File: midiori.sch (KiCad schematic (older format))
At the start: 48 parts, among them J1 x68000_expansion, J2 DIN-5_180degree, J3 DIN-5_180degree, J4 DIN-5_180degree, U1 74LS245, U10 74LS393, U11 74LS74, U13 H11L1, U14 7407, U15 74LS157, U2 74LS133, U3 74LS133, U4 74LS08, U5 74LS38, U6 ym3802-x, U7 74LS32, U8 74LS04, U9 74LS10, X1 CXO_DIP8, X2 CXO_DIP8

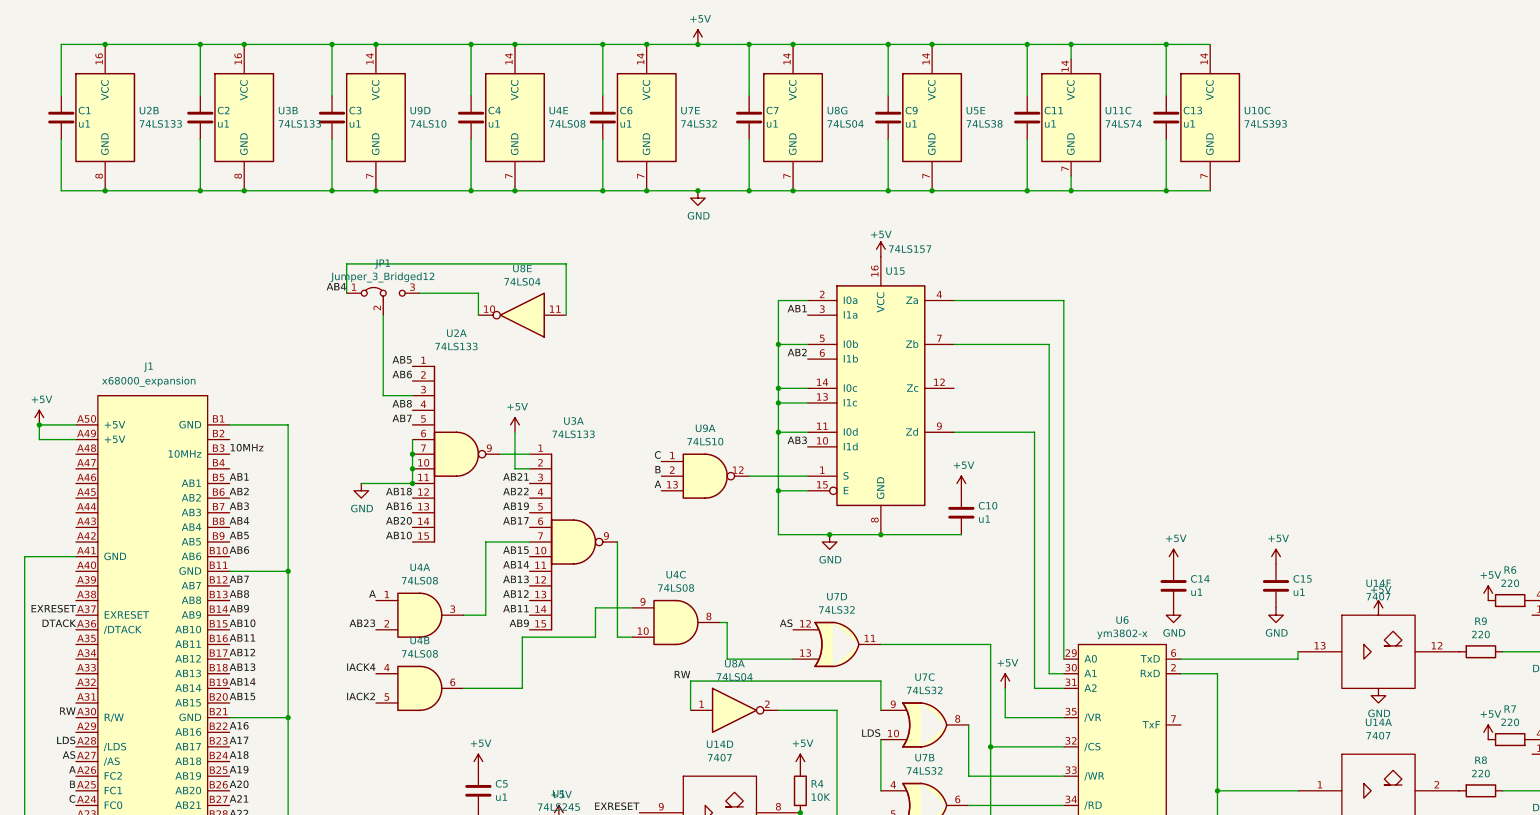
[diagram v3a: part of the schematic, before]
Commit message: Remove 74ls133 from address decoding
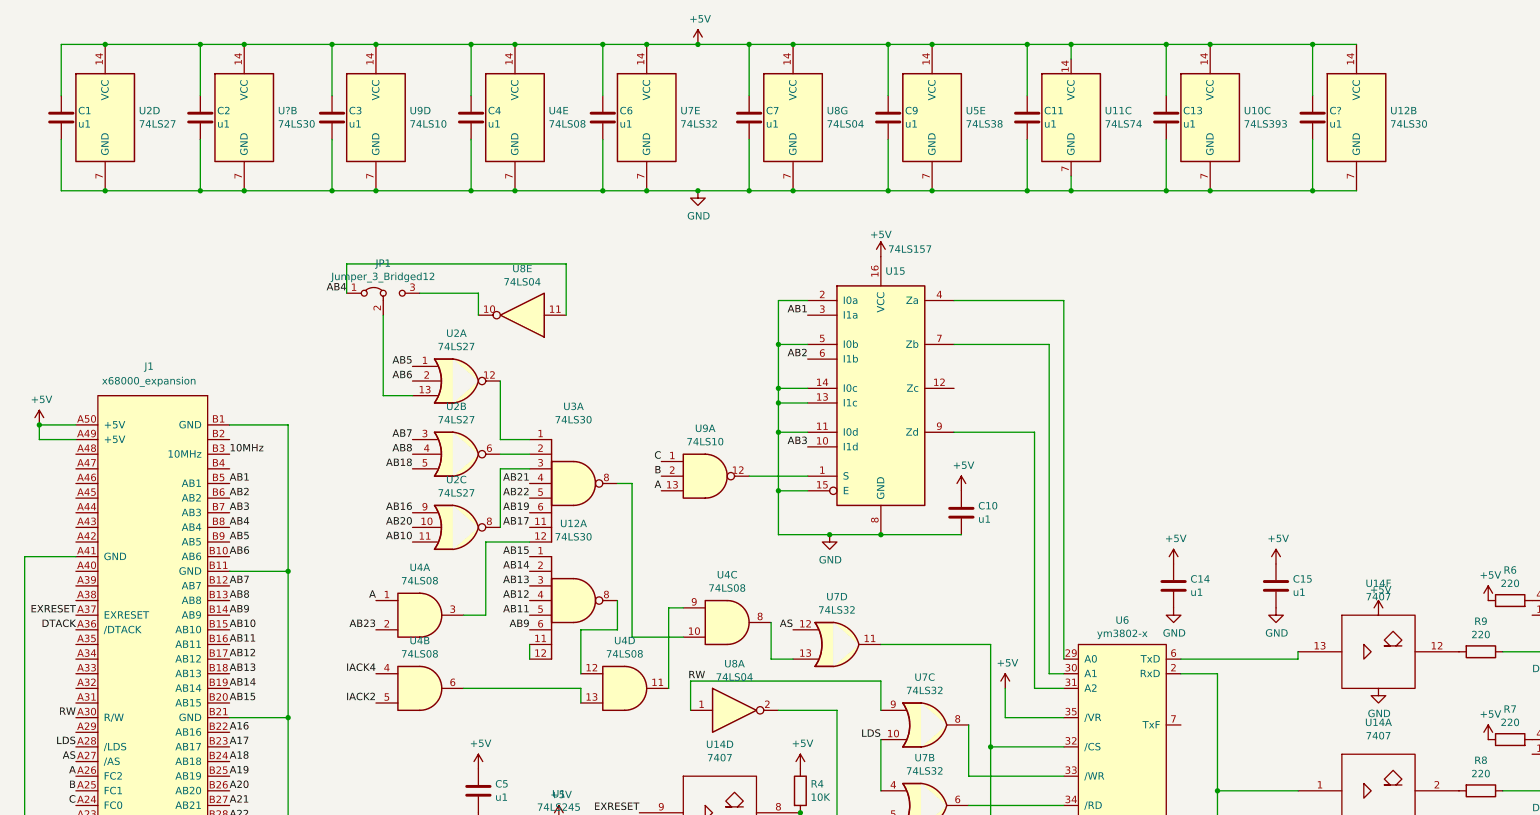
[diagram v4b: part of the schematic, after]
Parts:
- removed U2, U3: 74LS133, Package_SO:SOIC-16_3.9x9.9mm_P1.27mm, symbol 74xx:74LS133
- added C?: u1, Capacitor_SMD:C_0805_2012Metric_Pad1.15x1.40mm_HandSolder, symbol Device:C
- added U12, U3, U?: 74LS30, symbol 74xx:74LS30
- added U2: 74LS27, symbol 74xx:74LS27
- added unit 4 of U4
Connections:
- net +5V: now also C?.1, U12.14 (VCC), U2.14 (VCC), U?.14 (VCC)
- net AB10: now also U2.11
- net AB11: now also U12.5
- net AB12: now also U12.4
- net AB13: now also U12.3
- net AB14: now also U12.2
- net AB15: now also U12.1
- net AB16: now also U2.9
- net AB17: now also U3.11
- net AB18: now also U2.5
- net AB19: now also U3.6
- net AB20: now also U2.10
- net AB21: now also U3.4
- net AB22: now also U3.5
- net AB5: now also U2.1
- net AB6: now also U2.2
- net AB7: now also U2.3
- net AB8: now also U2.4
- net AB9: now also U12.6
- net GND: now also C?.2, U12.7 (GND), U2.7 (GND), U?.7 (GND)
- net at U4.3: now also U3.12
- net at U4.10: now also U3.8
- net at JP1.2 (C): now also U2.13
- net at U4.6: now also U4.13; no longer U4.9
- new net: U4.11, U4.9
- new net: U2.12, U3.1
- new net: U2.6, U3.2
- new net: U2.8, U3.3
- new net: U12.11, U12.12
- new net: U12.8, U4.12
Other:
- moved on the sheet: U4C
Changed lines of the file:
@@
 Text Label 4050 7050 2    50   ~ 0
 DB0
-$Comp
-L 74xx:74LS133 U3
-U 1 1 5BFE5824
-P 4650 4150
-F 0 "U3" H 4650 4975 50  0000 C CNN
-F 1 "74LS133" H 4650 4884 50  0000 C CNN
-F 2 "Package_SO:SOIC-16_3.9x9.9mm_P1.27mm" H 4650 4150 50  0001 C CNN
-F 3 "http://www.ti.com/lit/gpn/sn74LS133" H 4650 4150 50  0001 C CNN
-	1    4650 4150
-	1    0    0    -1
-$EndComp
-$Comp
-L 74xx:74LS133 U2
-U 2 1 5BFE5AAA
-P 1450 1250
-F 0 "U2" H 1680 1296 50  0000 L CNN
-F 1 "74LS133" H 1680 1205 50  0000 L CNN
-F 2 "Package_SO:SOIC-16_3.9x9.9mm_P1.27mm" H 1450 1250 50  0001 C CNN
-F 3 "http://www.ti.com/lit/gpn/sn74LS133" H 1450 1250 50  0001 C CNN
-	2    1450 1250
-	1    0    0    -1
-$EndComp
-$Comp
-L 74xx:74LS133 U2
-U 1 1 5BFE5C09
-P 3850 3550
-F 0 "U2" H 3850 4375 50  0000 C CNN
-F 1 "74LS133" H 3850 4284 50  0000 C CNN
-F 2 "Package_SO:SOIC-16_3.9x9.9mm_P1.27mm" H 3850 3550 50  0001 C CNN
-F 3 "http://www.ti.com/lit/gpn/sn74LS133" H 3850 3550 50  0001 C CNN
-	1    3850 3550
-	1    0    0    -1
-$EndComp
-$Comp
-L 74xx:74LS133 U3
-U 2 1 5BFE5CB5
-P 2400 1250
-F 0 "U3" H 2630 1296 50  0000 L CNN
-F 1 "74LS133" H 2630 1205 50  0000 L CNN
-F 2 "Package_SO:SOIC-16_3.9x9.9mm_P1.27mm" H 2400 1250 50  0001 C CNN
-F 3 "http://www.ti.com/lit/gpn/sn74LS133" H 2400 1250 50  0001 C CNN
-	2    2400 1250
-	1    0    0    -1
-$EndComp
 Text Label 3550 2950 2    50   ~ 0
 AB5
@@
 Text Label 3100 2450 2    50   ~ 0
 AB4
-Text Label 3550 3250 2    50   ~ 0
+Text Label 3550 3550 2    50   ~ 0
 AB8
-Text Label 3550 3350 2    50   ~ 0
+Text Label 3550 3450 2    50   ~ 0
 AB7
 Text Label 3550 4150 2    50   ~ 0
@@
 Text Label 3550 3950 2    50   ~ 0
 AB16
-Text Label 3550 3850 2    50   ~ 0
+Text Label 3550 3650 2    50   ~ 0
 AB18
 Wire Wire Line
-	3550 3450 3550 3550
-Wire Wire Line
-	3550 3650 3550 3550
-Connection ~ 3550 3550
-Wire Wire Line
-	3550 3750 3550 3650
-Connection ~ 3550 3650
-$Comp
-L power:GND #PWR0107
-U 1 1 5BFE694A
-P 3200 3750
-F 0 "#PWR0107" H 3200 3500 50  0001 C CNN
-F 1 "GND" H 3205 3577 50  0000 C CNN
-F 2 "" H 3200 3750 50  0001 C CNN
-F 3 "" H 3200 3750 50  0001 C CNN
-	1    3200 3750
-	1    0    0    -1
-$EndComp
-Wire Wire Line
-	3550 3750 3200 3750
-Connection ~ 3550 3750
-Wire Wire Line
 	4150 3550 4350 3550
-$Comp
-L power:+5V #PWR0108
-U 1 1 5BFE7542
-P 4250 3400
-F 0 "#PWR0108" H 4250 3250 50  0001 C CNN
-F 1 "+5V" H 4265 3573 50  0000 C CNN
-F 2 "" H 4250 3400 50  0001 C CNN
-F 3 "" H 4250 3400 50  0001 C CNN
-	1    4250 3400
-	1    0    0    -1
-$EndComp
-Wire Wire Line
-	4250 3400 4250 3650
-Wire Wire Line
-	4250 3650 4350 3650
 Text Label 4350 3750 2    50   ~ 0
 AB21
@@
 L 74xx:74LS08 U4
 U 3 1 5BFE9128
-P 5350 4700
-F 0 "U4" H 5350 5025 50  0000 C CNN
-F 1 "74LS08" H 5350 4934 50  0000 C CNN
-F 2 "Package_SO:SOIC-14_3.9x8.7mm_P1.27mm" H 5350 4700 50  0001 C CNN
-F 3 "http://www.ti.com/lit/gpn/sn74LS08" H 5350 4700 50  0001 C CNN
-	3    5350 4700
-	1    0    0    -1
-$EndComp
-Wire Wire Line
-	3900 5150 4300 5150
-Wire Wire Line
-	4300 5150 4300 4800
-Wire Wire Line
-	4300 4800 4800 4800
-Wire Wire Line
-	4800 4800 4800 4600
-Wire Wire Line
-	4800 4600 5050 4600
-Wire Wire Line
-	4950 4150 4950 4800
-Wire Wire Line
-	4950 4800 5050 4800
+P 5700 4700
+F 0 "U4" H 5700 5025 50  0000 C CNN
+F 1 "74LS08" H 5700 4934 50  0000 C CNN
+F 2 "Package_SO:SOIC-14_3.9x8.7mm_P1.27mm" H 5700 4700 50  0001 C CNN
+F 3 "http://www.ti.com/lit/gpn/sn74LS08" H 5700 4700 50  0001 C CNN
+	3    5700 4700
+	1    0    0    -1
+$EndComp
+Wire Wire Line
+	5300 5150 5300 4600
+Wire Wire Line
+	5300 4600 5400 4600
 $Comp
 L 74xx:74LS157 U15
@@
 $EndComp
 Wire Wire Line
-	5700 4700 5650 4700
-Wire Wire Line
-	6150 4950 5700 4950
-Wire Wire Line
-	5700 4950 5700 4700
+	6150 4950 6000 4950
+Wire Wire Line
+	6000 4950 6000 4700
 Text Label 6150 4750 2    50   ~ 0
 AS
@@
 Wire Wire Line
 	5450 5100 5450 5300
-Text Label 5450 5100 2    50   ~ 0
+Text Label 5550 5100 2    50   ~ 0
 RW
 $Comp
@@
 Wire Wire Line
 	1150 1400 1150 1750
-Wire Wire Line
-	1150 1750 1450 1750
-Connection ~ 1450 1750
-Wire Wire Line
-	1450 1750 2100 1750
 Connection ~ 3300 1750
 Wire Wire Line
 	3300 1750 3950 1750
-Connection ~ 2400 1750
-Wire Wire Line
-	2400 1750 3000 1750
 Connection ~ 4250 1750
 Wire Wire Line
@@
 Connection ~ 3300 750
 Wire Wire Line
-	2400 750  2100 750
-Connection ~ 2400 750
-Wire Wire Line
-	1450 750  1150 750
-Wire Wire Line
 	1150 750  1150 1100
-Connection ~ 1450 750
 $Comp
 L power:GND #PWR0135
@@
 	2100 1100 2100 750
 Connection ~ 2100 750
-Wire Wire Line
-	2100 750  1450 750
 Connection ~ 2100 1750
-Wire Wire Line
-	2100 1750 2400 1750
 Wire Wire Line
 	2100 1400 2100 1750
@@
 Connection ~ 3000 750
 Wire Wire Line
-	3000 750  2400 750
-Wire Wire Line
 	3000 1400 3000 1750
 Connection ~ 3000 1750
@@
 Wire Wire Line
 	8050 750  7750 750
+$Comp
+L 74xx:74LS27 U2
+U 1 1 5C02762B
+P 3850 3050
+F 0 "U2" H 3850 3375 50  0000 C CNN
+F 1 "74LS27" H 3850 3284 50  0000 C CNN
+F 2 "" H 3850 3050 50  0001 C CNN
+F 3 "http://www.ti.com/lit/gpn/sn74LS27" H 3850 3050 50  0001 C CNN
+	1    3850 3050
+	1    0    0    -1
+$EndComp
+$Comp
+L 74xx:74LS27 U2
+U 2 1 5C02913D
+P 3850 3550
+F 0 "U2" H 3850 3875 50  0000 C CNN
+F 1 "74LS27" H 3850 3784 50  0000 C CNN
+F 2 "" H 3850 3550 50  0001 C CNN
+F 3 "http://www.ti.com/lit/gpn/sn74LS27" H 3850 3550 50  0001 C CNN
+	2    3850 3550
+	1    0    0    -1
+$EndComp
+$Comp
+L 74xx:74LS27 U2
+U 3 1 5C02B75B
+P 3850 4050
+F 0 "U2" H 3850 4375 50  0000 C CNN
+F 1 "74LS27" H 3850 4284 50  0000 C CNN
+F 2 "" H 3850 4050 50  0001 C CNN
+F 3 "http://www.ti.com/lit/gpn/sn74LS27" H 3850 4050 50  0001 C CNN
+	3    3850 4050
+	1    0    0    -1
+$EndComp
+Wire Wire Line
+	4150 4050 4150 3650
+Wire Wire Line
+	4150 3650 4350 3650
+Wire Wire Line
+	1150 750  1450 750
+Wire Wire Line
+	1150 1750 1450 1750
+$Comp
+L 74xx:74LS27 U2
+U 4 1 5C03F9B7
+P 1450 1250
+F 0 "U2" H 1680 1296 50  0000 L CNN
+F 1 "74LS27" H 1680 1205 50  0000 L CNN
+F 2 "" H 1450 1250 50  0001 C CNN
+F 3 "http://www.ti.com/lit/gpn/sn74LS27" H 1450 1250 50  0001 C CNN
+	4    1450 1250
+	1    0    0    -1
+$EndComp
+Connection ~ 1450 750
+Wire Wire Line
+	1450 750  2100 750
+Connection ~ 1450 1750
+Wire Wire Line
+	1450 1750 2100 1750
+Wire Wire Line
+	2100 750  2400 750
+Wire Wire Line
+	2100 1750 2400 1750
+$Comp
+L 74xx:74LS30 U3
+U 1 1 5C0424B1
+P 4650 3750
+F 0 "U3" H 4650 4275 50  0000 C CNN
+F 1 "74LS30" H 4650 4184 50  0000 C CNN
+F 2 "" H 4650 3750 50  0001 C CNN
+F 3 "http://www.ti.com/lit/gpn/sn74LS30" H 4650 3750 50  0001 C CNN
+	1    4650 3750
+	1    0    0    -1
+$EndComp
+$Comp
+L 74xx:74LS30 U12
+U 1 1 5C0552C7
+P 4650 4550
+F 0 "U12" H 4650 5075 50  0000 C CNN
+F 1 "74LS30" H 4650 4984 50  0000 C CNN
+F 2 "" H 4650 4550 50  0001 C CNN
+F 3 "http://www.ti.com/lit/gpn/sn74LS30" H 4650 4550 50  0001 C CNN
+	1    4650 4550
+	1    0    0    -1
+$EndComp
+Wire Wire Line
+	4150 3050 4150 3450
+Wire Wire Line
+	4150 3450 4350 3450
+$Comp
+L 74xx:74LS08 U4
+U 4 1 5C0AD493
+P 5000 5150
+F 0 "U4" H 5000 5475 50  0000 C CNN
+F 1 "74LS08" H 5000 5384 50  0000 C CNN
+F 2 "" H 5000 5150 50  0001 C CNN
+F 3 "http://www.ti.com/lit/gpn/sn74LS08" H 5000 5150 50  0001 C CNN
+	4    5000 5150
+	1    0    0    -1
+$EndComp
+Wire Wire Line
+	4700 5050 4700 4750
+Wire Wire Line
+	4700 4750 4950 4750
+Wire Wire Line
+	4950 4750 4950 4550
+Wire Wire Line
+	3900 5150 4700 5150
+Wire Wire Line
+	4700 5150 4700 5250
+Wire Wire Line
+	5400 4800 5050 4800
+Wire Wire Line
+	5050 4800 5050 3750
+Wire Wire Line
+	5050 3750 4950 3750
+Wire Wire Line
+	4350 4850 4350 4950
+$Comp
+L 74xx:74LS30 U?
+U 2 1 5C14CD3F
+P 2400 1250
+F 0 "U?" H 2630 1296 50  0000 L CNN
+F 1 "74LS30" H 2630 1205 50  0000 L CNN
+F 2 "" H 2400 1250 50  0001 C CNN
+F 3 "http://www.ti.com/lit/gpn/sn74LS30" H 2400 1250 50  0001 C CNN
+	2    2400 1250
+	1    0    0    -1
+$EndComp
+Connection ~ 2400 750
+Wire Wire Line
+	2400 750  3000 750
+Connection ~ 2400 1750
+Wire Wire Line
+	2400 1750 3000 1750
+$Comp
+L 74xx:74LS30 U12
+U 2 1 5C14E02C
+P 10000 1250
+F 0 "U12" H 10230 1296 50  0000 L CNN
+F 1 "74LS30" H 10230 1205 50  0000 L CNN
+F 2 "" H 10000 1250 50  0001 C CNN
+F 3 "http://www.ti.com/lit/gpn/sn74LS30" H 10000 1250 50  0001 C CNN
+	2    10000 1250
+	1    0    0    -1
+$EndComp
+$Comp
+L Device:C C?
+U 1 1 5C14FD68
+P 9700 1250
+F 0 "C?" H 9815 1296 50  0000 L CNN
+F 1 "u1" H 9815 1205 50  0000 L CNN
+F 2 "Capacitor_SMD:C_0805_2012Metric_Pad1.15x1.40mm_HandSolder" H 9738 1100 50  0001 C CNN
+F 3 "~" H 9700 1250 50  0001 C CNN
+	1    9700 1250
+	1    0    0    -1
+$EndComp
+Wire Wire Line
+	9000 750  9700 750
+Connection ~ 9000 750
+Wire Wire Line
+	9000 1750 9700 1750
+Connection ~ 9000 1750
+Wire Wire Line
+	9700 1400 9700 1750
+Connection ~ 9700 1750
+Wire Wire Line
+	9700 1750 10000 1750
+Wire Wire Line
+	9700 1100 9700 750
+Connection ~ 9700 750
+Wire Wire Line
+	9700 750  10000 750
 $EndSCHEMATC

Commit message: more
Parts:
- removed C15, C2: u1, Capacitor_SMD:C_0805_2012Metric_Pad1.15x1.40mm_HandSolder, symbol Device:C
- removed U?: 74LS30, symbol 74xx:74LS30
- J1: symbol midiori-rescue:x68000_expansion-x68k -> midiori-rescue:x68000_expansion-x68k-midiori-rescue
- U12, U2, U3: footprint (none) -> Package_SO:SOIC-14_3.9x8.7mm_P1.27mm
- U6: symbol midiori-rescue:ym3802-x-x68k -> midiori-rescue:ym3802-x-x68k-midiori-rescue
- X1: value CXO_DIP8 -> 16MHz; footprint Oscillator:Oscillator_DIP-8 -> Oscillator:Oscillator_SMD_SeikoEpson_SG8002CA-4Pin_7.0x5.0mm; symbol Oscillator:CXO_DIP8 -> x68k:SG5032CAN
- X2: value CXO_DIP8 -> 4.9152MHz; footprint Oscillator:Oscillator_DIP-8 -> Oscillator:Oscillator_SMD_SeikoEpson_SG8002CA-4Pin_7.0x5.0mm; symbol Oscillator:CXO_DIP8 -> x68k:SG5032CAN
- gave numbers to parts that had none: 1
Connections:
- net +5V: now also X1.4 (V+), X2.4 (V+); no longer X1.8 (Vcc), X2.8 (Vcc)
- net GND: now also X1.2 (GND), X2.2 (GND); no longer X1.4 (GND), X2.4 (GND)
- net at U10.1 (CP): now also X1.3 (OUT); no longer X1.5 (OUT)
- net at U10.13 (CP): now also X2.3 (OUT); no longer X2.5 (OUT)
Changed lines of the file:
@@
 $EndDescr
 $Comp
-L midiori-rescue:x68000_expansion-x68k J1
+L midiori-rescue:x68000_expansion-x68k-midiori-rescue J1
 U 1 1 5BFF029F
 P 2150 -1050
@@
 AS
 $Comp
-L midiori-rescue:ym3802-x-x68k U6
+L midiori-rescue:ym3802-x-x68k-midiori-rescue U6
 U 1 1 5BFF5246
 P 8100 4850
@@
 RW
 $Comp
-L Oscillator:CXO_DIP8 X1
-U 1 1 5C01CB41
-P 6550 9450
-F 0 "X1" H 6891 9496 50  0000 L CNN
-F 1 "CXO_DIP8" H 6891 9405 50  0000 L CNN
-F 2 "Oscillator:Oscillator_DIP-8" H 7000 9100 50  0001 C CNN
-F 3 "http://cdn-reichelt.de/documents/datenblatt/B400/OSZI.pdf" H 6450 9450 50  0001 C CNN
-	1    6550 9450
-	1    0    0    -1
-$EndComp
-$Comp
-L Oscillator:CXO_DIP8 X2
+L x68k:SG5032CAN X2
 U 1 1 5C01D210
 P 9050 9450
 F 0 "X2" H 9391 9496 50  0000 L CNN
-F 1 "CXO_DIP8" H 9391 9405 50  0000 L CNN
-F 2 "Oscillator:Oscillator_DIP-8" H 9500 9100 50  0001 C CNN
+F 1 "4.9152MHz" H 9391 9405 50  0000 L CNN
+F 2 "Oscillator:Oscillator_SMD_SeikoEpson_SG8002CA-4Pin_7.0x5.0mm" H 9500 9100 50  0001 C CNN
 F 3 "http://cdn-reichelt.de/documents/datenblatt/B400/OSZI.pdf" H 8950 9450 50  0001 C CNN
 	1    9050 9450
@@
 Wire Wire Line
 	6250 9150 6550 9150
-Connection ~ 6550 9150
 $Comp
 L power:GND #PWR0122
@@
 $EndComp
 $Comp
-L Device:C C2
-U 1 1 5C2379F1
-P 2100 1250
-F 0 "C2" H 2215 1296 50  0000 L CNN
-F 1 "u1" H 2215 1205 50  0000 L CNN
-F 2 "Capacitor_SMD:C_0805_2012Metric_Pad1.15x1.40mm_HandSolder" H 2138 1100 50  0001 C CNN
-F 3 "~" H 2100 1250 50  0001 C CNN
-	1    2100 1250
-	1    0    0    -1
-$EndComp
-$Comp
 L Device:C C3
 U 1 1 5C237E3F
@@
 Wire Wire Line
 	5500 750  5850 750
-Wire Wire Line
-	2100 1100 2100 750
-Connection ~ 2100 750
-Connection ~ 2100 1750
-Wire Wire Line
-	2100 1400 2100 1750
 $Comp
 L power:GND #PWR0137
@@
 	1    0    0    -1
 $EndComp
-$Comp
-L Device:C C15
-U 1 1 5C3357D0
-P 9450 4450
-F 0 "C15" H 9565 4496 50  0000 L CNN
-F 1 "u1" H 9565 4405 50  0000 L CNN
-F 2 "Capacitor_SMD:C_0805_2012Metric_Pad1.15x1.40mm_HandSolder" H 9488 4300 50  0001 C CNN
-F 3 "~" H 9450 4450 50  0001 C CNN
-	1    9450 4450
-	1    0    0    -1
-$EndComp
-$Comp
-L power:GND #PWR0139
-U 1 1 5C335BF0
-P 9450 4600
-F 0 "#PWR0139" H 9450 4350 50  0001 C CNN
-F 1 "GND" H 9455 4427 50  0000 C CNN
-F 2 "" H 9450 4600 50  0001 C CNN
-F 3 "" H 9450 4600 50  0001 C CNN
-	1    9450 4600
-	1    0    0    -1
-$EndComp
-$Comp
-L power:+5V #PWR0140
-U 1 1 5C342736
-P 9450 4300
-F 0 "#PWR0140" H 9450 4150 50  0001 C CNN
-F 1 "+5V" H 9465 4473 50  0000 C CNN
-F 2 "" H 9450 4300 50  0001 C CNN
-F 3 "" H 9450 4300 50  0001 C CNN
-	1    9450 4300
-	1    0    0    -1
-$EndComp
 Wire Wire Line
 	3000 1100 3000 750
@@
 Wire Wire Line
 	6000 9750 6000 9600
-Connection ~ 6550 9750
 Wire Wire Line
 	6000 9300 6000 9150
@@
 F 0 "U2" H 3850 3375 50  0000 C CNN
 F 1 "74LS27" H 3850 3284 50  0000 C CNN
-F 2 "" H 3850 3050 50  0001 C CNN
+F 2 "Package_SO:SOIC-14_3.9x8.7mm_P1.27mm" H 3850 3050 50  0001 C CNN
 F 3 "http://www.ti.com/lit/gpn/sn74LS27" H 3850 3050 50  0001 C CNN
 	1    3850 3050
@@
 F 0 "U2" H 3850 3875 50  0000 C CNN
 F 1 "74LS27" H 3850 3784 50  0000 C CNN
-F 2 "" H 3850 3550 50  0001 C CNN
+F 2 "Package_SO:SOIC-14_3.9x8.7mm_P1.27mm" H 3850 3550 50  0001 C CNN
 F 3 "http://www.ti.com/lit/gpn/sn74LS27" H 3850 3550 50  0001 C CNN
 	2    3850 3550
@@
 F 0 "U2" H 3850 4375 50  0000 C CNN
 F 1 "74LS27" H 3850 4284 50  0000 C CNN
-F 2 "" H 3850 4050 50  0001 C CNN
+F 2 "Package_SO:SOIC-14_3.9x8.7mm_P1.27mm" H 3850 4050 50  0001 C CNN
 F 3 "http://www.ti.com/lit/gpn/sn74LS27" H 3850 4050 50  0001 C CNN
 	3    3850 4050
@@
 F 0 "U2" H 1680 1296 50  0000 L CNN
 F 1 "74LS27" H 1680 1205 50  0000 L CNN
-F 2 "" H 1450 1250 50  0001 C CNN
+F 2 "Package_SO:SOIC-14_3.9x8.7mm_P1.27mm" H 1450 1250 50  0001 C CNN
 F 3 "http://www.ti.com/lit/gpn/sn74LS27" H 1450 1250 50  0001 C CNN
 	4    1450 1250
@@
 $EndComp
 Connection ~ 1450 750
-Wire Wire Line
-	1450 750  2100 750
 Connection ~ 1450 1750
-Wire Wire Line
-	1450 1750 2100 1750
-Wire Wire Line
-	2100 750  2400 750
-Wire Wire Line
-	2100 1750 2400 1750
 $Comp
 L 74xx:74LS30 U3
@@
 F 0 "U3" H 4650 4275 50  0000 C CNN
 F 1 "74LS30" H 4650 4184 50  0000 C CNN
-F 2 "" H 4650 3750 50  0001 C CNN
+F 2 "Package_SO:SOIC-14_3.9x8.7mm_P1.27mm" H 4650 3750 50  0001 C CNN
 F 3 "http://www.ti.com/lit/gpn/sn74LS30" H 4650 3750 50  0001 C CNN
 	1    4650 3750
@@
 F 0 "U12" H 4650 5075 50  0000 C CNN
 F 1 "74LS30" H 4650 4984 50  0000 C CNN
-F 2 "" H 4650 4550 50  0001 C CNN
+F 2 "Package_SO:SOIC-14_3.9x8.7mm_P1.27mm" H 4650 4550 50  0001 C CNN
 F 3 "http://www.ti.com/lit/gpn/sn74LS30" H 4650 4550 50  0001 C CNN
 	1    4650 4550
@@
 	4350 4850 4350 4950
 $Comp
-L 74xx:74LS30 U?
-U 2 1 5C14CD3F
-P 2400 1250
-F 0 "U?" H 2630 1296 50  0000 L CNN
-F 1 "74LS30" H 2630 1205 50  0000 L CNN
-F 2 "" H 2400 1250 50  0001 C CNN
-F 3 "http://www.ti.com/lit/gpn/sn74LS30" H 2400 1250 50  0001 C CNN
-	2    2400 1250
-	1    0    0    -1
-$EndComp
-Connection ~ 2400 750
-Wire Wire Line
-	2400 750  3000 750
-Connection ~ 2400 1750
-Wire Wire Line
-	2400 1750 3000 1750
-$Comp
 L 74xx:74LS30 U12
 U 2 1 5C14E02C
@@
 F 0 "U12" H 10230 1296 50  0000 L CNN
 F 1 "74LS30" H 10230 1205 50  0000 L CNN
-F 2 "" H 10000 1250 50  0001 C CNN
+F 2 "Package_SO:SOIC-14_3.9x8.7mm_P1.27mm" H 10000 1250 50  0001 C CNN
 F 3 "http://www.ti.com/lit/gpn/sn74LS30" H 10000 1250 50  0001 C CNN
 	2    10000 1250
@@
 $EndComp
 $Comp
-L Device:C C?
+L Device:C C17
 U 1 1 5C14FD68
 P 9700 1250
-F 0 "C?" H 9815 1296 50  0000 L CNN
+F 0 "C17" H 9815 1296 50  0000 L CNN
 F 1 "u1" H 9815 1205 50  0000 L CNN
 F 2 "Capacitor_SMD:C_0805_2012Metric_Pad1.15x1.40mm_HandSolder" H 9738 1100 50  0001 C CNN
@@
 Wire Wire Line
 	9700 750  10000 750
+Wire Wire Line
+	1450 750  3000 750
+Wire Wire Line
+	1450 1750 3000 1750
+Connection ~ 6550 9150
+Connection ~ 6550 9750
+$Comp
+L x68k:SG5032CAN X1
+U 1 1 5C01CB41
+P 6550 9450
+F 0 "X1" H 6891 9496 50  0000 L CNN
+F 1 "16MHz" H 6891 9405 50  0000 L CNN
+F 2 "Oscillator:Oscillator_SMD_SeikoEpson_SG8002CA-4Pin_7.0x5.0mm" H 7000 9100 50  0001 C CNN
+F 3 "http://cdn-reichelt.de/documents/datenblatt/B400/OSZI.pdf" H 6450 9450 50  0001 C CNN
+	1    6550 9450
+	1    0    0    -1
+$EndComp
 $EndSCHEMATC
